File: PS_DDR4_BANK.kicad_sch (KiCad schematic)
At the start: 1 part, among them U13 XCZU15EG-2FFVB1156E

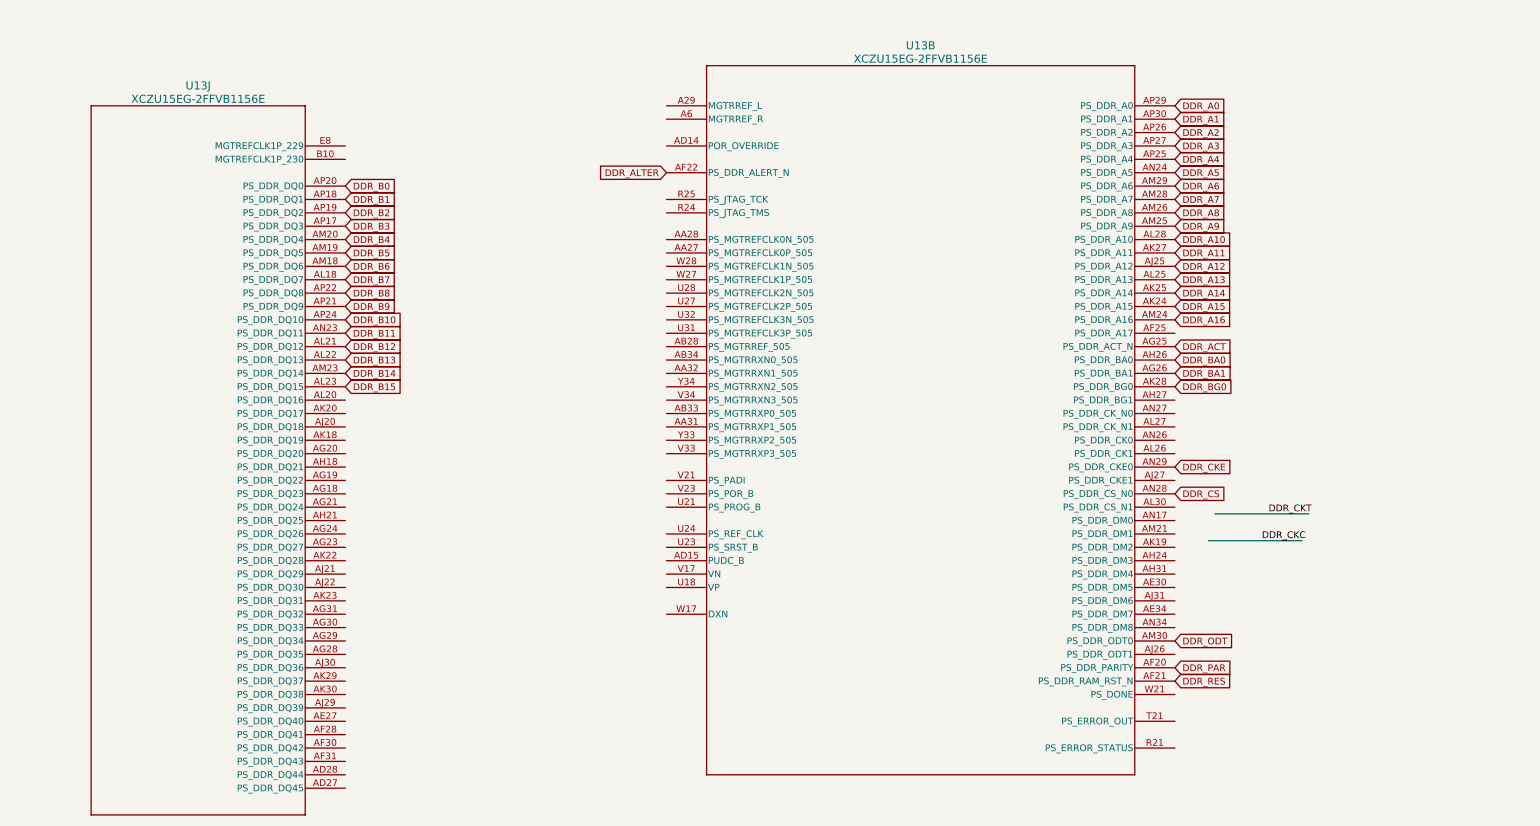
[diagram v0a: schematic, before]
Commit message: DDR4 added
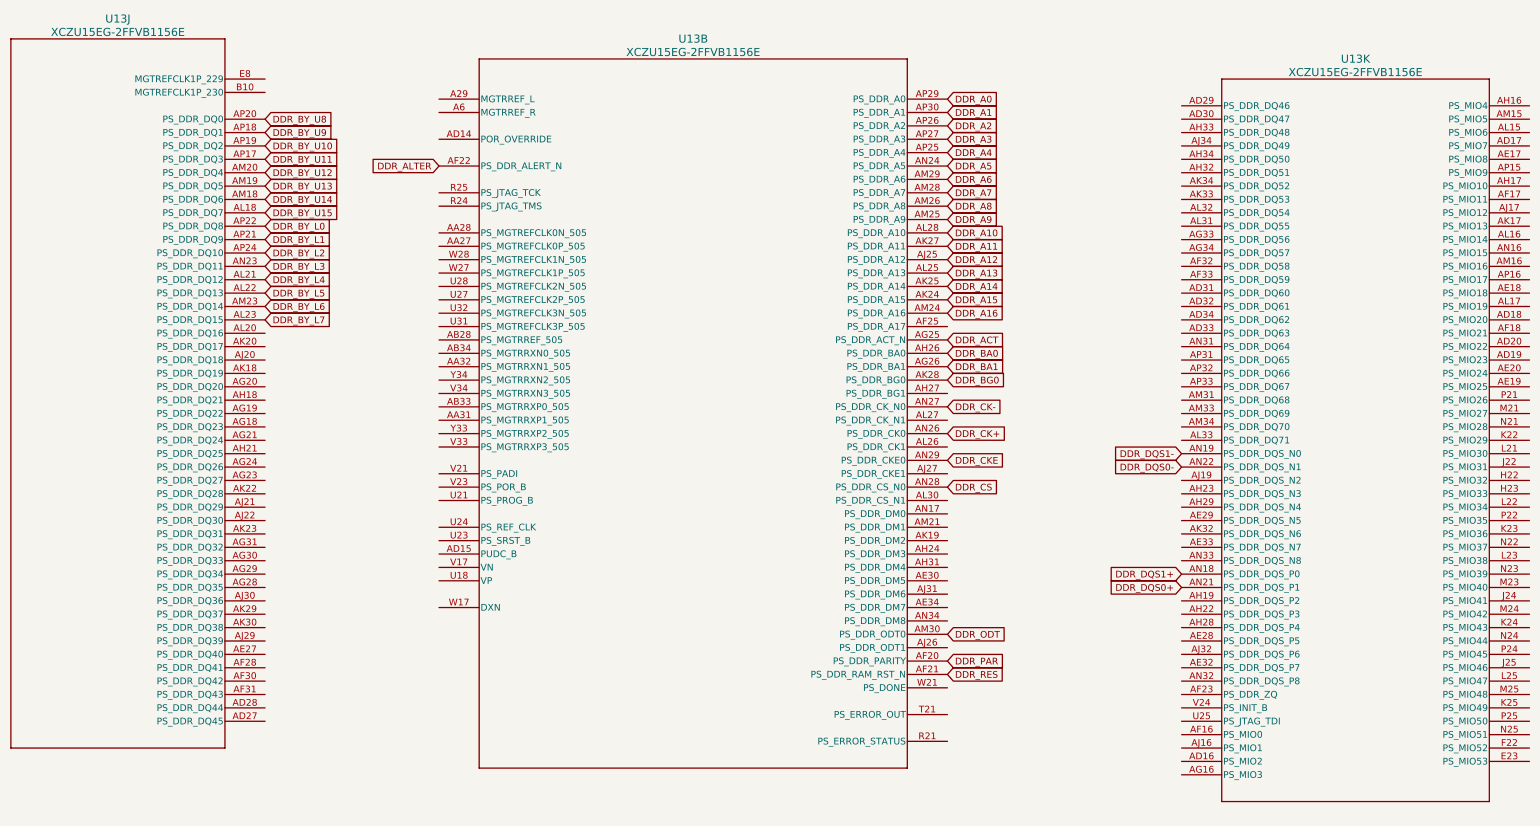
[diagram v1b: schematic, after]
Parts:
- added unit 11 of U13
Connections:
- net DDR_CK+: now reaches U13.AN26 (PS_DDR_CK0)
- net DDR_CK-: now reaches U13.AN27 (PS_DDR_CK_N0)
- net DDR_B0 renamed DDR_BY_U8
- net DDR_B1 renamed DDR_BY_U9
- net DDR_B10 renamed DDR_BY_L2
- net DDR_B11 renamed DDR_BY_L3
- net DDR_B12 renamed DDR_BY_L4
- net DDR_B13 renamed DDR_BY_L5
- net DDR_B14 renamed DDR_BY_L6
- net DDR_B15 renamed DDR_BY_L7
- net DDR_B2 renamed DDR_BY_U10
- net DDR_B3 renamed DDR_BY_U11
- net DDR_B4 renamed DDR_BY_U12
- net DDR_B5 renamed DDR_BY_U13
- net DDR_B6 renamed DDR_BY_U14
- net DDR_B7 renamed DDR_BY_U15
- net DDR_B8 renamed DDR_BY_L0
- net DDR_B9 renamed DDR_BY_L1
- new net DDR_DQS0+: U13.AN21 (PS_DDR_DQS_P1)
- new net DDR_DQS0-: U13.AN22 (PS_DDR_DQS_N1)
- new net DDR_DQS1+: U13.AN18 (PS_DDR_DQS_P0)
- new net DDR_DQS1-: U13.AN19 (PS_DDR_DQS_N0)
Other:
- moved on the sheet: U13B, U13J
